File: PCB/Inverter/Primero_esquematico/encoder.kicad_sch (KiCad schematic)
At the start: 15 parts, among them J9 430451218, U24 AM26LS32AIDR, U25 SN65HVD82DR, U26 SN74LVC245ANSR

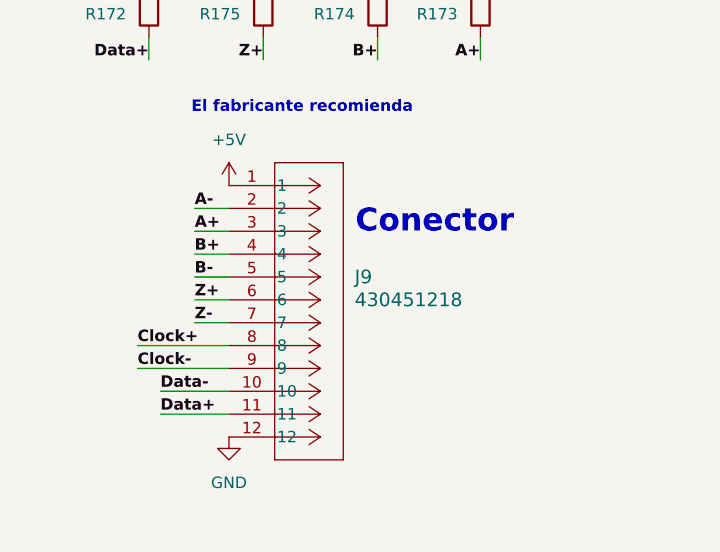
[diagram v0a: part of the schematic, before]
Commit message: Un par de cosas q corregi del ERC pero sigue mal
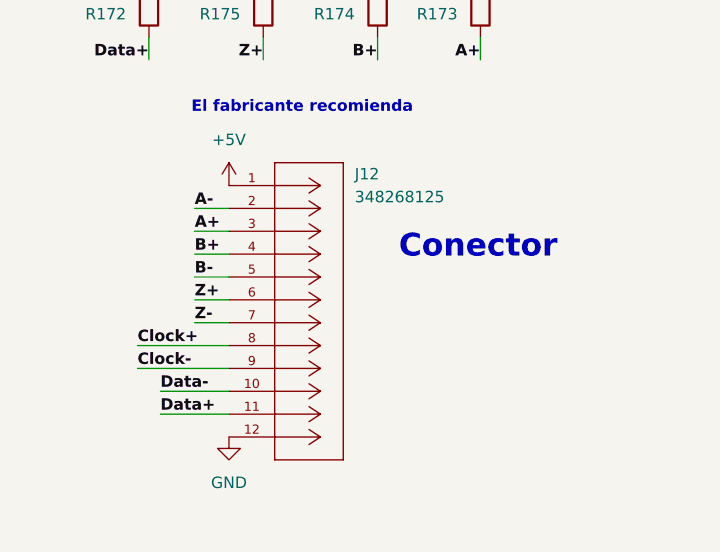
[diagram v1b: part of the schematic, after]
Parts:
- removed J9: 430451218, Snapeda:CONN_SD-43045-007_12_MOL, symbol Snapeda:430451218
- added J12: 348268125, Snapeda:CONN_SD-34826-001_12_MOL, symbol Snapeda:348268125
- U24: footprint Snapeda:D16-L -> D16
- U25: footprint Snapeda:D8_TEX-L -> D8_TEX
- U26: footprint Snapeda:NS20-L -> NS20
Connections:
- net +5V: now also J12.1
- net A+: now also J12.3
- net A-: now also J12.2
- net B+: now also J12.4
- net B-: now also J12.5
- net Clock+: now also J12.8
- net Clock-: now also J12.9
- net Data+: now also J12.11
- net Data-: now also J12.10
- net GND: now also J12.12
- net Z+: now also J12.6
- net Z-: now also J12.7
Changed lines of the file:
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@@
 	(text "Conector"
 		(exclude_from_sim no)
-		(at 241.3 132.334 0)
+		(at 246.126 135.128 0)
 		(effects
 			(font
@@
 			)
 		)
-		(property "Footprint" "Snapeda:D16-L"
+		(property "Footprint" "D16"
 			(at 104.14 82.55 0)
 			(hide yes)
@@
 	)
 	(symbol
-		(lib_id "Snapeda:430451218")
-		(at 218.44 128.27 0)
-		(unit 1)
-		(body_style 1)
-		(exclude_from_sim no)
-		(in_bom yes)
-		(on_board yes)
-		(in_pos_files yes)
-		(dnp no)
-		(fields_autoplaced yes)
-		(property "Reference" "J9"
-			(at 232.41 138.4299 0)
-			(show_name no)
-			(do_not_autoplace no)
-			(effects
-				(font
-					(size 1.524 1.524)
-				)
-				(justify left)
-			)
-		)
-		(property "Value" "430451218"
-			(at 232.41 140.9699 0)
-			(show_name no)
-			(do_not_autoplace no)
-			(effects
-				(font
-					(size 1.524 1.524)
-				)
-				(justify left)
-			)
-		)
-		(property "Footprint" "Snapeda:CONN_SD-43045-007_12_MOL"
-			(at 232.41 143.5099 0)
-			(hide yes)
-			(show_name no)
-			(do_not_autoplace no)
-			(effects
-				(font
-					(size 1.27 1.27)
-				)
-				(justify left)
-			)
-		)
-		(property "Datasheet" "https://www.molex.com/en-us/products/part-detail-pdf/430451218?display=pdf"
-			(at 232.41 146.0499 0)
-			(hide yes)
-			(show_name no)
-			(do_not_autoplace no)
-			(effects
-				(font
-					(size 1.27 1.27)
-				)
-				(justify left)
-			)
-		)
-		(property "Description" ""
-			(at 218.44 128.27 0)
-			(hide yes)
-			(show_name no)
-			(do_not_autoplace no)
-			(effects
-				(font
-					(size 1.27 1.27)
-				)
-			)
-		)
-		(property "Compra" "https://www.digikey.com/es/products/detail/molex/0430451218/5043826"
-			(at 218.44 128.27 0)
-			(hide yes)
-			(show_name no)
-			(do_not_autoplace no)
-			(effects
-				(font
-					(size 1.27 1.27)
-				)
-			)
-		)
-		(pin "1"
-		)
-		(pin "8"
-		)
-		(pin "2"
-		)
-		(pin "3"
-		)
-		(pin "4"
-		)
-		(pin "5"
-		)
-		(pin "6"
-		)
-		(pin "7"
-		)
-		(pin "10"
-		)
-		(pin "11"
-		)
-		(pin "12"
-		)
-		(pin "9"
-		)
-		(instances
-			(project "Primero_esquematico"
-				(path "/d930f486-f6ac-489c-907e-47f2cb34cf04/0bcc01e0-1903-49c9-8a02-17640b3194e7/68d930cc-b92a-410a-8391-4213b1f3804b"
-					(reference "J9")
-					(unit 1)
-				)
-			)
-		)
-	)
-	(symbol
 		(lib_id "power:+5V")
 		(at 130.81 57.15 0)
@@
 			)
 		)
-		(property "Description" "-- valores mixtos --"
+		(property "Description" "Resistor"
 			(at 209.55 107.95 0)
 			(hide yes)
@@
 	)
 	(symbol
+		(lib_id "Snapeda:348268125")
+		(at 218.44 128.27 0)
+		(unit 1)
+		(body_style 1)
+		(exclude_from_sim no)
+		(in_bom yes)
+		(on_board yes)
+		(in_pos_files yes)
+		(dnp no)
+		(fields_autoplaced yes)
+		(property "Reference" "J12"
+			(at 232.41 126.9999 0)
+			(show_name no)
+			(do_not_autoplace no)
+			(effects
+				(font
+					(size 1.27 1.27)
+				)
+				(justify left)
+			)
+		)
+		(property "Value" "348268125"
+			(at 232.41 129.5399 0)
+			(show_name no)
+			(do_not_autoplace no)
+			(effects
+				(font
+					(size 1.27 1.27)
+				)
+				(justify left)
+			)
+		)
+		(property "Footprint" "Snapeda:CONN_SD-34826-001_12_MOL"
+			(at 232.41 132.0799 0)
+			(hide yes)
+			(show_name no)
+			(do_not_autoplace no)
+			(effects
+				(font
+					(size 1.27 1.27)
+				)
+				(justify left)
+			)
+		)
+		(property "Datasheet" ""
+			(at 218.44 128.27 0)
+			(hide yes)
+			(show_name no)
+			(do_not_autoplace no)
+			(effects
+				(font
+					(size 1.27 1.27)
+				)
+			)
+		)
+		(property "Description" "Conn Shrouded Header (4 Sides) HDR 12 POS 2mm Solder RA Side Entry Thru-Hole T/R"
+			(at 232.41 134.6199 0)
+			(hide yes)
+			(show_name no)
+			(do_not_autoplace no)
+			(effects
+				(font
+					(size 1.27 1.27)
+				)
+				(justify left)
+			)
+		)
+		(property "MF" "Molex"
+			(at 232.41 137.1599 0)
+			(hide yes)
+			(show_name no)
+			(do_not_autoplace no)
+			(effects
+				(font
+					(size 1.27 1.27)
+				)
+				(justify left)
+			)
+		)
+		(property "Package" "None"
+			(at 232.41 139.6999 0)
+			(hide yes)
+			(show_name no)
+			(do_not_autoplace no)
+			(effects
+				(font
+					(size 1.27 1.27)
+				)
+				(justify left)
+			)
+		)
+		(property "Price" "None"
+			(at 232.41 142.2399 0)
+			(hide yes)
+			(show_name no)
+			(do_not_autoplace no)
+			(effects
+				(font
+					(size 1.27 1.27)
+				)
+				(justify left)
+			)
+		)
+		(property "Check_prices" "https://www.snapeda.com/parts/348268125/Molex/view-part/?ref=eda"
+			(at 232.41 144.7799 0)
+			(hide yes)
+			(show_name no)
+			(do_not_autoplace no)
+			(effects
+				(font
+					(size 1.27 1.27)
+				)
+				(justify left)
+			)
+		)
+		(property "Availability" "In Stock"
+			(at 232.41 147.3199 0)
+			(hide yes)
+			(show_name no)
+			(do_not_autoplace no)
+			(effects
+				(font
+					(size 1.27 1.27)
+				)
+				(justify left)
+			)
+		)
+		(property "SnapEDA_Link" "https://www.snapeda.com/parts/348268125/Molex/view-part/?ref=snap"
+			(at 232.41 149.8599 0)
+			(hide yes)
+			(show_name no)
+			(do_not_autoplace no)
+			(effects
+				(font
+					(size 1.27 1.27)
+				)
+				(justify left)
+			)
+		)
+		(property "MP" "348268125"
+			(at 232.41 152.3999 0)
+			(hide yes)
+			(show_name no)
+			(do_not_autoplace no)
+			(effects
+				(font
+					(size 1.27 1.27)
+				)
+				(justify left)
+			)
+		)
+		(property "MFR_NAME" "Molex Connector Corporation"
+			(at 232.41 154.9399 0)
+			(hide yes)
+			(show_name no)
+			(do_not_autoplace no)
+			(effects
+				(font
+					(size 1.27 1.27)
+				)
+				(justify left)
+			)
+		)
+		(property "MANUFACTURER_PART_NUMBER" "348268125"
+			(at 232.41 157.4799 0)
+			(hide yes)
+			(show_name no)
+			(do_not_autoplace no)
+			(effects
+				(font
+					(size 1.27 1.27)
+				)
+				(justify left)
+			)
+		)
+		(property "Compra" "https://www.mouser.com/ProductDetail/Molex/34826-8125?qs=5aG0NVq1C4wcrmMhGN6zIA%3D%3D&srsltid=AfmBOorqLlKMPlVU6ZP8HmmWWCI5S19idtaxZ42zIR8MsuWy_uqZq0st"
+			(at 218.44 128.27 0)
+			(hide yes)
+			(show_name no)
+			(do_not_autoplace no)
+			(effects
+				(font
+					(size 1.27 1.27)
+				)
+			)
+		)
+		(pin "1"
+		)
+		(pin "12"
+		)
+		(pin "4"
+		)
+		(pin "11"
+		)
+		(pin "3"
+		)
+		(pin "8"
+		)
+		(pin "10"
+		)
+		(pin "9"
+		)
+		(pin "5"
+		)
+		(pin "7"
+		)
+		(pin "2"
+		)
+		(pin "6"
+		)
+		(instances
+			(project "Primero_esquematico"
+				(path "/d930f486-f6ac-489c-907e-47f2cb34cf04/0bcc01e0-1903-49c9-8a02-17640b3194e7/68d930cc-b92a-410a-8391-4213b1f3804b"
+					(reference "J12")
+					(unit 1)
+				)
+			)
+		)
+	)
+	(symbol
 		(lib_id "power:+5V")
 		(at 218.44 128.27 0)
@@
 			)
 		)
-		(property "Footprint" "Snapeda:D8_TEX-L"
+		(property "Footprint" "D8_TEX"
 			(at 102.87 46.99 0)
 			(hide yes)
@@
 			)
 		)
-		(property "Footprint" "Snapeda:NS20-L"
+		(property "Footprint" "NS20"
 			(at 105.41 124.46 0)
 			(hide yes)
@@
 			)
 		)
-		(property "Description" "-- valores mixtos --"
+		(property "Description" "Resistor"
 			(at 143.51 63.5 0)
 			(hide yes)
@@
 			)
 		)
-		(property "Description" "-- valores mixtos --"
+		(property "Description" "Resistor"
 			(at 246.38 107.95 0)
 			(hide yes)
@@
 			)
 		)
-		(property "Description" "-- valores mixtos --"
+		(property "Description" "Resistor"
 			(at 222.25 107.95 0)
 			(hide yes)
@@
 			)
 		)
-		(property "Description" "-- valores mixtos --"
+		(property "Description" "Resistor"
 			(at 71.12 52.07 0)
 			(hide yes)
@@
 			)
 		)
-		(property "Description" "-- valores mixtos --"
+		(property "Description" "Resistor"
 			(at 234.95 107.95 0)
 			(hide yes)

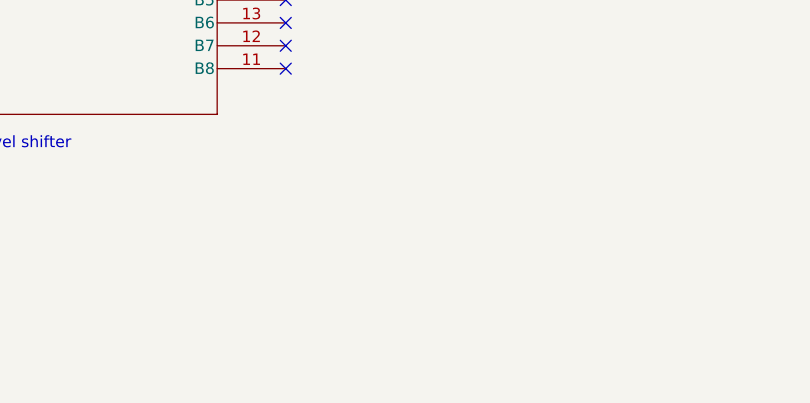
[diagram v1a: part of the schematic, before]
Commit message: Esquematico Listo
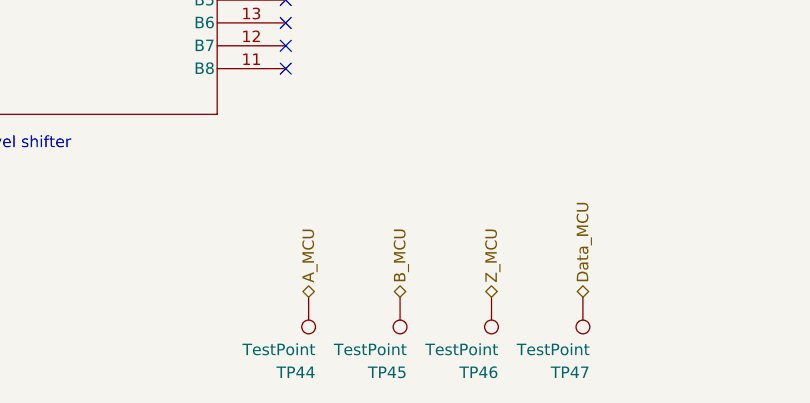
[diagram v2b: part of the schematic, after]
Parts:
- added TP44, TP45, TP46, TP47: TestPoint, TestPoint:TestPoint_Pad_D2.0mm, symbol Connector:TestPoint
- U24: footprint D16 -> Snapeda:D16-L
- U25: footprint D8_TEX -> NuevoGui:D8_TEX-L
- U26: footprint NS20 -> Snapeda:NS20-L
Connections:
- net A_MCU: now also TP44.1
- net B_MCU: now also TP45.1
- net Data_MCU: now also TP47.1
- net Z_MCU: now also TP46.1

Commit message: correcciones
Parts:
- added C136, C137: 100nF, Capacitor_SMD:C_0603_1608Metric, symbol Device:C
- R196: renamed from R181; footprint Resistor_SMD:R_0402_1005Metric -> Resistor_SMD:R_0603_1608Metric
- TP41: renamed from TP44; footprint TestPoint:TestPoint_Pad_D2.0mm -> TestPoint:TestPoint_Pad_D1.0mm
- TP42: renamed from TP45; footprint TestPoint:TestPoint_Pad_D2.0mm -> TestPoint:TestPoint_Pad_D1.0mm
- TP43: renamed from TP46; footprint TestPoint:TestPoint_Pad_D2.0mm -> TestPoint:TestPoint_Pad_D1.0mm
- TP44: renamed from TP47; footprint TestPoint:TestPoint_Pad_D2.0mm -> TestPoint:TestPoint_Pad_D1.0mm
- renumbered C81 to C135, C82 to C138, C85 to C139, C84 to C140, C83 to C141, J12 to J5, R171 to R197, R172 to R198, R175 to R199, R174 to R200, R173 to R201, U25 to U34, U24 to U35, U26 to U36
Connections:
- net +5V: now also C136.1, C137.1
- net GND: now also C136.2, C137.2

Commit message: Algunos cambios
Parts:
- removed J5: 348268125, Snapeda:CONN_SD-34826-001_12_MOL, symbol Snapeda:348268125
- added J2: 348250125, Snapeda:CONN_SD-34825-001_12_MOL, symbol Snapeda:348250125
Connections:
- net +5V: now also J2.1
- net A+: now also J2.3
- net A-: now also J2.2
- net B+: now also J2.4
- net B-: now also J2.5
- net Clock+: now also J2.8
- net Clock-: now also J2.9
- net Data+: now also J2.11
- net Data-: now also J2.10
- net GND: now also J2.12
- net Z+: now also J2.6
- net Z-: now also J2.7
- net +3.3V renamed +3.3_digital

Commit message: Corregi cosas de la placa
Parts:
- renumbered C135 to C155, C136 to C156, C137 to C157, C138 to C158, C139 to C159, C140 to C160, C141 to C161, J2 to J6, U34 to U33, U35 to U34, U36 to U35

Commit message: a
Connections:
- net +5V: no longer C156.1, C157.1, R196.2, U33.8 (VCC), U34.16 (VCC), U34.4 (G)
- new net +5V_digital: C156.1, C157.1, R196.2, U33.8 (VCC), U34.16 (VCC), U34.4 (G)
